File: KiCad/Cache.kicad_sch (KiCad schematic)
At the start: 25 parts, among them U801 61C256-15, U802 61C1024-20, U803 61C1024-20, U804 61C1024-20, U805 61C1024-20, U806 61C256-15, U807 61C256-15, U808 61C256-15, U809 61C256-15, U810 74F08

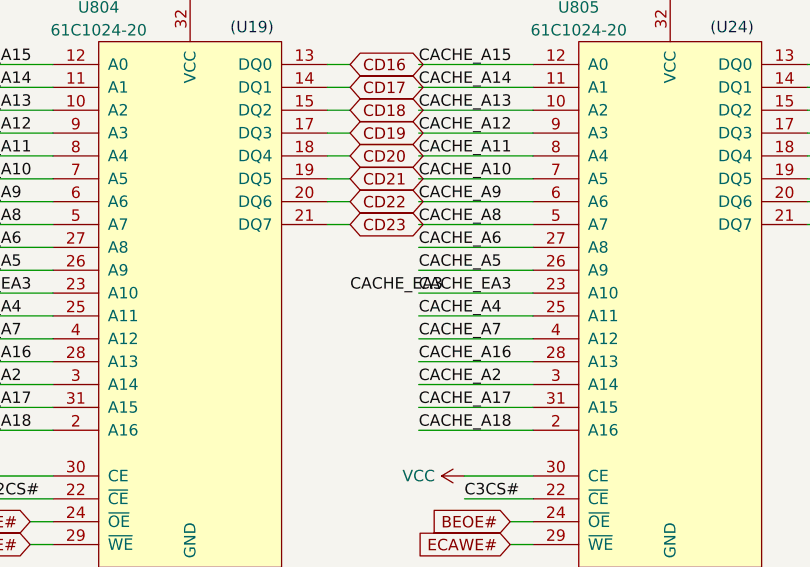
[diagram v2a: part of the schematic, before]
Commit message: Version 0.4: Update chipset connection
Signed-off-by: Sergey Kiselev <skiselev@gmail.com>
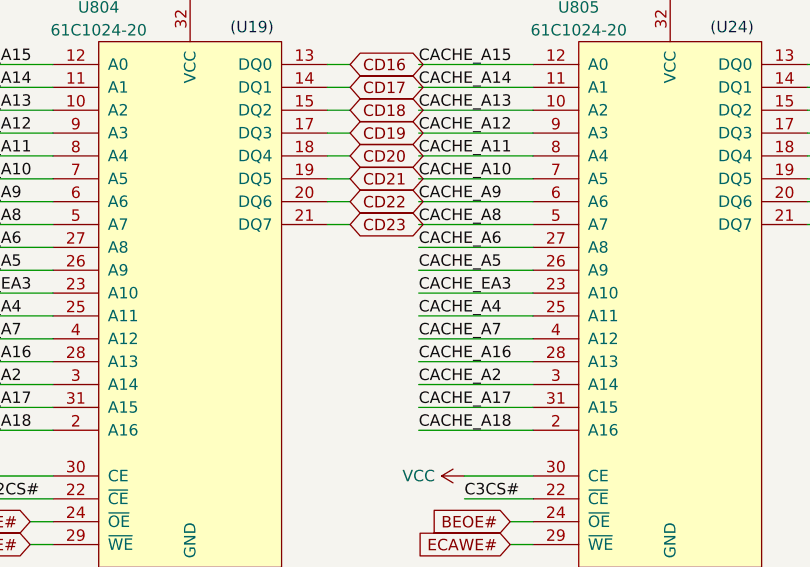
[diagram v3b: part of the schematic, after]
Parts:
- JP801, JP802: footprint (none) -> My_Components:Conn_Pin_Header_3x1_2.54mm
- JP803, JP804, JP805: footprint (none) -> My_Components:Conn_Pin_Header_2x1_2.54mm
- R801, R802, R803, R804, R805, R806, R807: footprint (none) -> Resistor_SMD:R_0612_1632Metric_Pad1.18x3.40mm_HandSolder
- RN801, RN802, RN803: footprint (none) -> Resistor_THT:R_Array_SIP8
- U801, U806, U807, U808, U809: footprint (none) -> My_Components:IC_DIP28_300
- U802, U803, U804, U805: footprint (none) -> My_Components:IC_DIP32_600
- U810: footprint (none) -> My_Components:IC_DIP14_300
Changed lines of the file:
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@@
-    (effects (font (size 1.27 1.27)) (justify left bottom))
-  )
-  (label "CACHE_EA3" (at 220.98 50.8 0)
     (effects (font (size 1.27 1.27)) (justify left bottom))
   )
@@
       (effects (font (size 1.524 1.524)))
     )
-    (property "Footprint" "" (id 2) (at 40.64 53.34 0)
+    (property "Footprint" "My_Components:IC_DIP28_300" (id 2) (at 40.64 53.34 0)
       (effects (font (size 1.524 1.524)) hide)
     )
@@
     (property "Reference" "U802" (id 0) (at 86.36 19.05 0))
     (property "Value" "61C1024-20" (id 1) (at 86.36 21.59 0))
-    (property "Footprint" "" (id 2) (at 96.52 53.34 0)
+    (property "Footprint" "My_Components:IC_DIP32_600" (id 2) (at 96.52 53.34 0)
       (effects (font (size 1.524 1.524)) hide)
     )
@@
     (property "Reference" "U803" (id 0) (at 139.7 19.05 0))
     (property "Value" "61C1024-20" (id 1) (at 139.7 21.59 0))
-    (property "Footprint" "" (id 2) (at 149.86 53.34 0)
+    (property "Footprint" "My_Components:IC_DIP32_600" (id 2) (at 149.86 53.34 0)
       (effects (font (size 1.524 1.524)) hide)
     )
@@
     (property "Reference" "U804" (id 0) (at 193.04 19.05 0))
     (property "Value" "61C1024-20" (id 1) (at 193.04 21.59 0))
-    (property "Footprint" "" (id 2) (at 203.2 53.34 0)
+    (property "Footprint" "My_Components:IC_DIP32_600" (id 2) (at 203.2 53.34 0)
       (effects (font (size 1.524 1.524)) hide)
     )
@@
     (property "Reference" "U805" (id 0) (at 246.38 19.05 0))
     (property "Value" "61C1024-20" (id 1) (at 246.38 21.59 0))
-    (property "Footprint" "" (id 2) (at 256.54 53.34 0)
+    (property "Footprint" "My_Components:IC_DIP32_600" (id 2) (at 256.54 53.34 0)
       (effects (font (size 1.524 1.524)) hide)
     )
@@
     (property "Reference" "U810" (id 0) (at 38.1 184.785 0))
     (property "Value" "74F08" (id 1) (at 38.1 187.0964 0))
-    (property "Footprint" "" (id 2) (at 38.1 193.04 0)
+    (property "Footprint" "My_Components:IC_DIP14_300" (id 2) (at 38.1 193.04 0)
       (effects (font (size 1.27 1.27)) hide)
     )
@@
     (property "Reference" "U810" (id 0) (at 152.4 184.785 0))
     (property "Value" "74F08" (id 1) (at 152.4 187.0964 0))
-    (property "Footprint" "" (id 2) (at 152.4 193.04 0)
+    (property "Footprint" "My_Components:IC_DIP14_300" (id 2) (at 152.4 193.04 0)
       (effects (font (size 1.27 1.27)) hide)
     )
@@
     (property "Reference" "U810" (id 0) (at 114.3 184.785 0))
     (property "Value" "74F08" (id 1) (at 114.3 187.0964 0))
-    (property "Footprint" "" (id 2) (at 114.3 193.04 0)
+    (property "Footprint" "My_Components:IC_DIP14_300" (id 2) (at 114.3 193.04 0)
       (effects (font (size 1.27 1.27)) hide)
     )
@@
     (property "Reference" "U810" (id 0) (at 76.2 184.785 0))
     (property "Value" "74F08" (id 1) (at 76.2 187.0964 0))
-    (property "Footprint" "" (id 2) (at 76.2 193.04 0)
+    (property "Footprint" "My_Components:IC_DIP14_300" (id 2) (at 76.2 193.04 0)
       (effects (font (size 1.27 1.27)) hide)
     )
@@
       (effects (font (size 1.524 1.524)))
     )
-    (property "Footprint" "" (id 2) (at 152.4 134.62 0)
+    (property "Footprint" "My_Components:IC_DIP28_300" (id 2) (at 152.4 134.62 0)
       (effects (font (size 1.524 1.524)) hide)
     )
@@
       (effects (font (size 1.524 1.524)))
     )
-    (property "Footprint" "" (id 2) (at 205.74 134.62 0)
+    (property "Footprint" "My_Components:IC_DIP28_300" (id 2) (at 205.74 134.62 0)
       (effects (font (size 1.524 1.524)) hide)
     )
@@
       (effects (font (size 1.524 1.524)))
     )
-    (property "Footprint" "" (id 2) (at 256.54 134.62 0)
+    (property "Footprint" "My_Components:IC_DIP28_300" (id 2) (at 256.54 134.62 0)
       (effects (font (size 1.524 1.524)) hide)
     )
@@
       (effects (font (size 1.524 1.524)))
     )
-    (property "Footprint" "" (id 2) (at 99.06 134.62 0)
+    (property "Footprint" "My_Components:IC_DIP28_300" (id 2) (at 99.06 134.62 0)
       (effects (font (size 1.524 1.524)) hide)
     )
@@
     (property "Reference" "JP802" (id 0) (at 44.45 98.9584 0))
     (property "Value" "8K/32K or 16K  Tag Size" (id 1) (at 44.45 101.2698 0))
-    (property "Footprint" "" (id 2) (at 44.45 104.14 0)
+    (property "Footprint" "My_Components:Conn_Pin_Header_3x1_2.54mm" (id 2) (at 44.45 104.14 0)
       (effects (font (size 1.27 1.27)) hide)
     )
@@
     (property "Reference" "JP801" (id 0) (at 34.29 86.2584 0))
     (property "Value" "One/Two Cache Banks" (id 1) (at 34.29 88.5698 0))
-    (property "Footprint" "" (id 2) (at 34.29 91.44 0)
+    (property "Footprint" "My_Components:Conn_Pin_Header_3x1_2.54mm" (id 2) (at 34.29 91.44 0)
       (effects (font (size 1.27 1.27)) hide)
     )
@@
       (effects (font (size 1.27 1.27)) (justify left))
     )
-    (property "Footprint" "" (id 2) (at 42.672 141.605 90)
+    (property "Footprint" "Resistor_SMD:R_0612_1632Metric_Pad1.18x3.40mm_HandSolder" (id 2) (at 42.672 141.605 90)
       (effects (font (size 1.27 1.27)) hide)
     )
@@
     (property "Reference" "RN801" (id 0) (at 71.12 83.82 90))
     (property "Value" "22" (id 1) (at 71.12 86.36 90))
-    (property "Footprint" "" (id 2) (at 71.12 100.965 90)
+    (property "Footprint" "Resistor_THT:R_Array_SIP8" (id 2) (at 71.12 100.965 90)
       (effects (font (size 1.27 1.27)) hide)
     )
@@
     (property "Reference" "JP805" (id 0) (at 30.48 161.29 0))
     (property "Value" "Cache A16" (id 1) (at 30.48 163.83 0))
-    (property "Footprint" "" (id 2) (at 30.48 167.64 0)
+    (property "Footprint" "My_Components:Conn_Pin_Header_2x1_2.54mm" (id 2) (at 30.48 167.64 0)
       (effects (font (size 1.27 1.27)) hide)
     )
@@
     (property "Reference" "R805" (id 0) (at 54.61 106.68 90))
     (property "Value" "22" (id 1) (at 59.69 106.68 90))
-    (property "Footprint" "" (id 2) (at 57.15 105.918 90)
+    (property "Footprint" "Resistor_SMD:R_0612_1632Metric_Pad1.18x3.40mm_HandSolder" (id 2) (at 57.15 105.918 90)
       (effects (font (size 1.27 1.27)) hide)
     )
@@
       (effects (font (size 1.27 1.27)) (justify left))
     )
-    (property "Footprint" "" (id 2) (at 42.672 161.925 90)
+    (property "Footprint" "Resistor_SMD:R_0612_1632Metric_Pad1.18x3.40mm_HandSolder" (id 2) (at 42.672 161.925 90)
       (effects (font (size 1.27 1.27)) hide)
     )
@@
       (effects (font (size 1.27 1.27)) (justify left))
     )
-    (property "Footprint" "" (id 2) (at 42.672 121.285 90)
+    (property "Footprint" "Resistor_SMD:R_0612_1632Metric_Pad1.18x3.40mm_HandSolder" (id 2) (at 42.672 121.285 90)
       (effects (font (size 1.27 1.27)) hide)
     )
@@
     (property "Reference" "JP804" (id 0) (at 30.48 140.97 0))
     (property "Value" "Cache A17" (id 1) (at 30.48 143.51 0))
-    (property "Footprint" "" (id 2) (at 30.48 147.32 0)
+    (property "Footprint" "My_Components:Conn_Pin_Header_2x1_2.54mm" (id 2) (at 30.48 147.32 0)
       (effects (font (size 1.27 1.27)) hide)
     )
@@
     (property "Reference" "R804" (id 0) (at 31.75 106.68 90))
     (property "Value" "22" (id 1) (at 31.75 109.22 90))
-    (property "Footprint" "" (id 2) (at 31.75 105.918 90)
+    (property "Footprint" "Resistor_SMD:R_0612_1632Metric_Pad1.18x3.40mm_HandSolder" (id 2) (at 31.75 105.918 90)
       (effects (font (size 1.27 1.27)) hide)
     )
@@
     (property "Reference" "R807" (id 0) (at 115.57 170.18 90))
     (property "Value" "1k" (id 1) (at 120.65 170.18 90))
-    (property "Footprint" "" (id 2) (at 118.11 169.418 90)
+    (property "Footprint" "Resistor_SMD:R_0612_1632Metric_Pad1.18x3.40mm_HandSolder" (id 2) (at 118.11 169.418 90)
       (effects (font (size 1.27 1.27)) hide)
     )
@@
     (property "Reference" "R806" (id 0) (at 77.47 170.18 90))
     (property "Value" "10" (id 1) (at 82.55 170.18 90))
-    (property "Footprint" "" (id 2) (at 80.01 169.418 90)
+    (property "Footprint" "Resistor_SMD:R_0612_1632Metric_Pad1.18x3.40mm_HandSolder" (id 2) (at 80.01 169.418 90)
       (effects (font (size 1.27 1.27)) hide)
     )
@@
     (property "Reference" "JP803" (id 0) (at 30.48 120.65 0))
     (property "Value" "Cache A18" (id 1) (at 30.48 123.19 0))
-    (property "Footprint" "" (id 2) (at 30.48 127 0)
+    (property "Footprint" "My_Components:Conn_Pin_Header_2x1_2.54mm" (id 2) (at 30.48 127 0)
       (effects (font (size 1.27 1.27)) hide)
     )
@@
     (property "Reference" "RN803" (id 0) (at 177.8 83.82 90))
     (property "Value" "22" (id 1) (at 177.8 86.36 90))
-    (property "Footprint" "" (id 2) (at 177.8 100.965 90)
+    (property "Footprint" "Resistor_THT:R_Array_SIP8" (id 2) (at 177.8 100.965 90)
       (effects (font (size 1.27 1.27)) hide)
     )
@@
     (property "Reference" "RN802" (id 0) (at 124.46 83.82 90))
     (property "Value" "22" (id 1) (at 124.46 86.36 90))
-    (property "Footprint" "" (id 2) (at 124.46 100.965 90)
-      (effects (font (size 1.27 1.27)) hide)
-    )
+    (property "Footprint" "Resistor_THT:R_Array_SIP8" (id 2) (at 124.46 100.965 90)
+      (effects (font (size 1.27 1.27)) hide)
+    )
